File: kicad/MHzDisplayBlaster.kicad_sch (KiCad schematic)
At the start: 9 parts, among them J1 Conn_02x15 DigitLHS, J2 Conn_02x15 DigitRHS, J3 Conn_01x03_Pin, J4 Conn_01x02_Pin, U1 DC56-11GWA, U2 74LS04

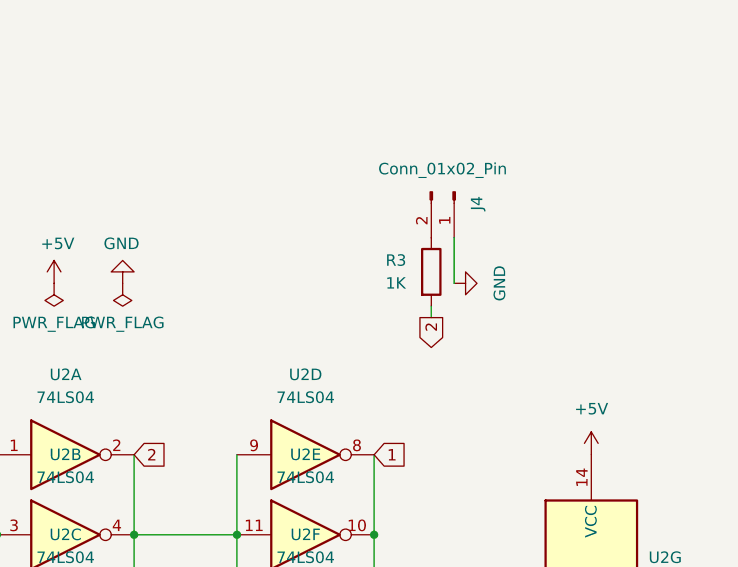
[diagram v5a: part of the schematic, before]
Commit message: Change HEX Inverter position, clean up layout
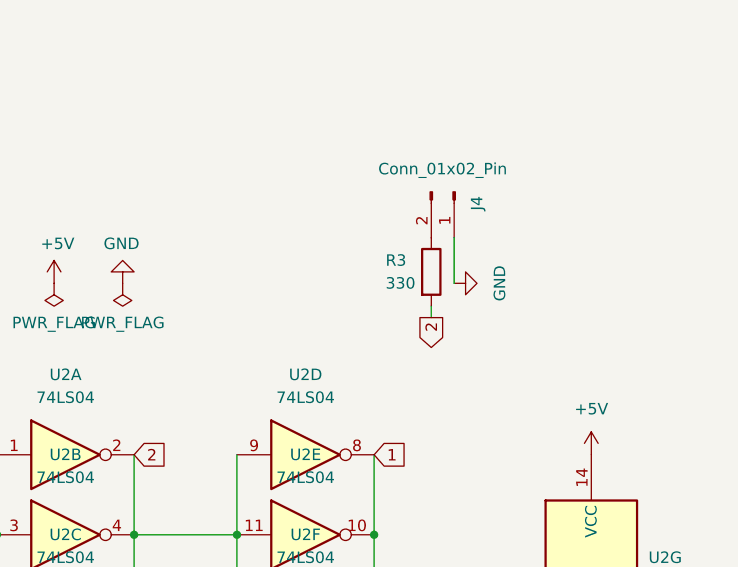
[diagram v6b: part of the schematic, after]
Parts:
- R3: value 1K -> 330
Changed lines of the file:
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@@
       (effects (font (size 1.27 1.27)) (justify left))
     )
-    (property "Value" "1K" (at 246.38 97.79 0)
+    (property "Value" "330" (at 246.38 97.79 0)
       (effects (font (size 1.27 1.27)) (justify left))
     )
